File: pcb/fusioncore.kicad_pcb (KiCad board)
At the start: 2 copper layers, 95 x 99 mm, 116 parts, among them J1 40HAT, J10 Pump_Misc_1, J11 Pump_Misc_2, J12 I2C_DBG, J13 Conn_02x03_Top_Bottom, J14 LED, J15 Trigger, J16 WEIGHT, J17 Valve_M1, J18 Valve_M2, J19 Valve_M3, J2 Conn_02x12_Top_Bottom, J20 Valve_M4, J21 Valve_Air_Lime, J22 Valve_Air_Rum, J23 Valve_Air_Out, J3 Flow_Warm, J4 Temperature, J5 Flow_Cold, J6 CONN_01X02, J7 Pump_Cold, J8 Pump_Warm, J9 Pump_Air, Q1 DMG2305UX, Q10 AO3400A, Q11 AO3400A, Q2 DMMT5401, Q3 AO3400A, Q4 AO3400A, Q5 AO3400A, Q6 AO3400A, Q7 AO3400A, Q8 MMBT4403, Q9 AO3400A, SW1 POWER_ON, U1 CAT24C32, U2 INA226, U3 INA226, U4 INA226, U5 TXB0108DQSR, U6 HX711, U7 P82B96

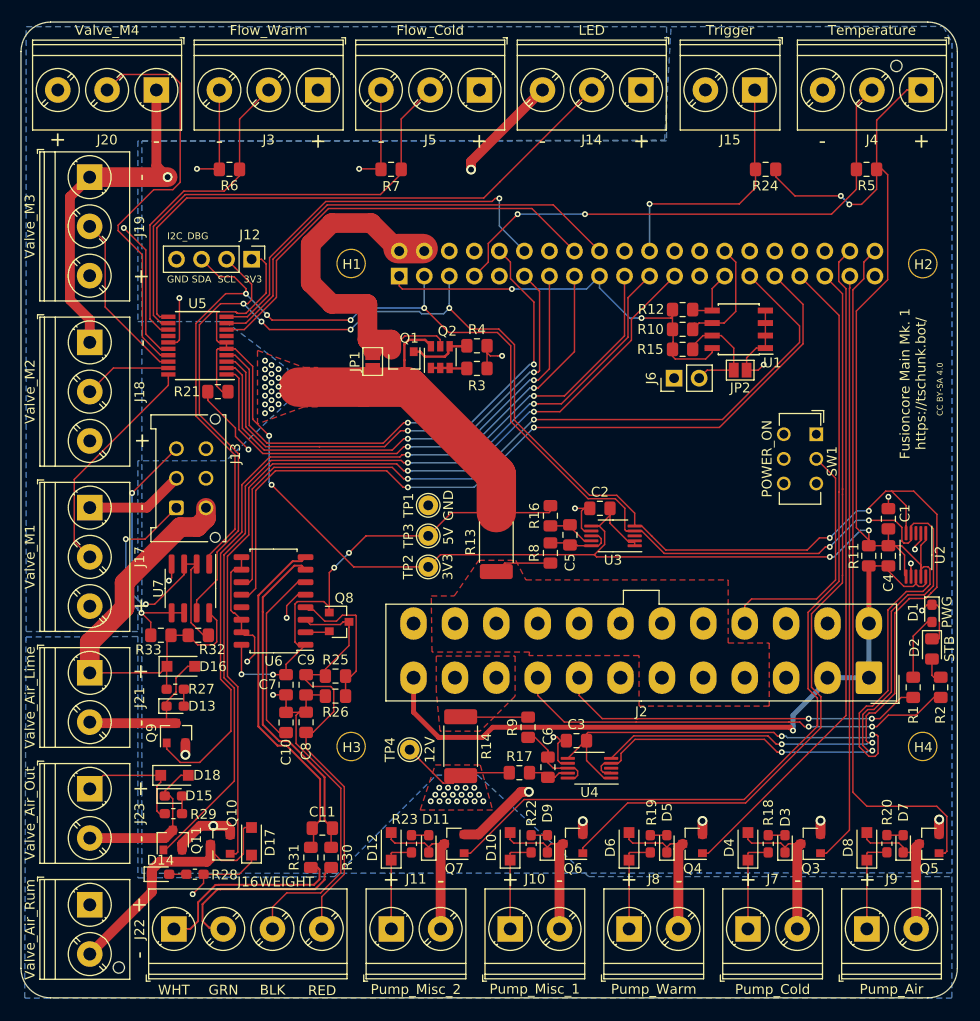
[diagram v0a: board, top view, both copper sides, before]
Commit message: Fixed issues from review.
Swapped diodes for Schottky diodes.
Changed logic level from HX711 to 3V3
Moved OE from 5V shifter to raspberry pi.
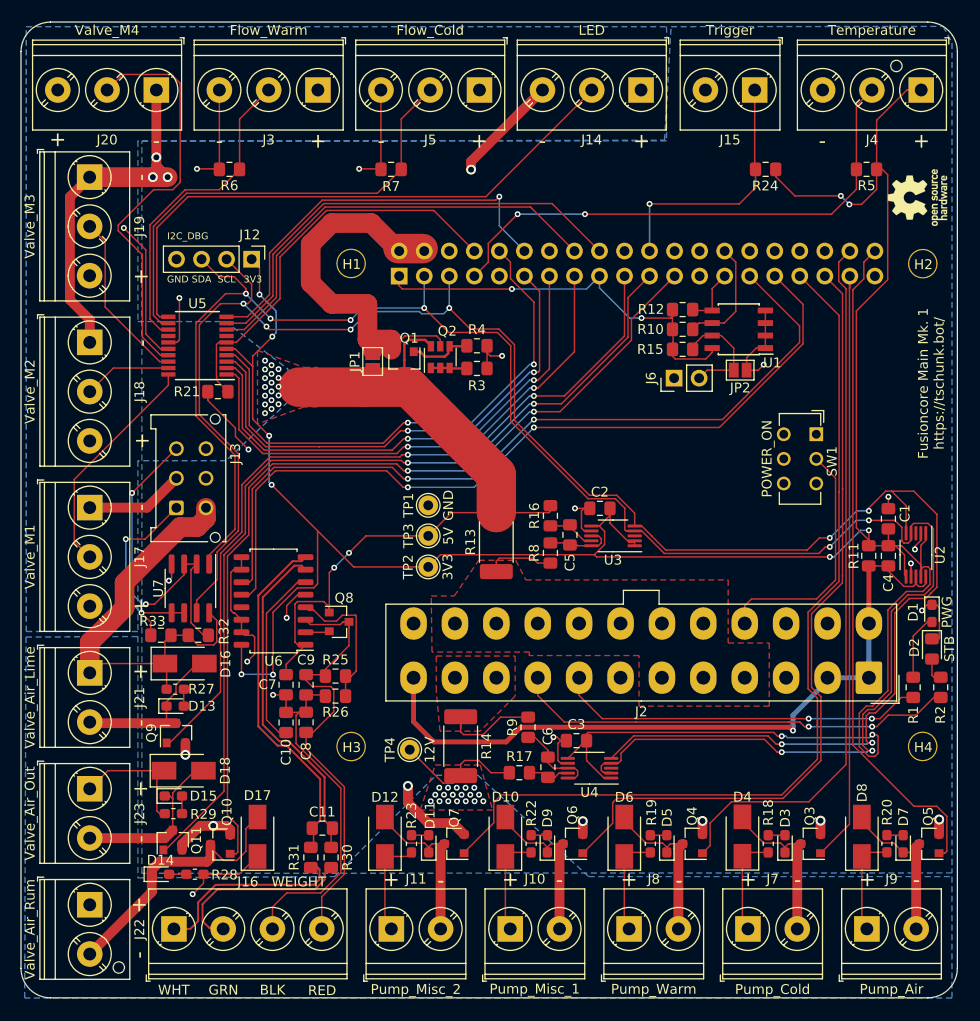
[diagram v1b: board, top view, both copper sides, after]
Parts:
- added REF**: OSHW-Logo_5.7x6mm_SilkScreen, Symbol:OSHW-Logo_5.7x6mm_SilkScreen, F.Cu at (139.5, 57.6)
- D10, D12, D16, D17, D18, D4, D6, D8: footprint Diode_SMD:D_SOD-123F -> Diode_SMD:D_SMA
- R1: value 150 -> 100
- moved D12 1.16 mm to (85.5, 122.5)
- moved D4 1.14 mm to (121.7, 122.5)
- moved D8 1.10 mm to (133.9, 122.5)
- moved D10 1.09 mm to (97.7, 122.5)
- moved D6 1.09 mm to (109.8, 122.5)
- moved D18 1.05 mm to (65.1, 115.8)
- moved D17 0.77 mm to (72.5, 122.5)
- moved D16 0.48 mm to (65.2, 104.9)
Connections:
- J1 pad 8: (no net) -> /EN_5V
- R21 pad 2: /3V3 -> /EN_5V
- U5 pad 6: /3V3 -> /EN_5V
- U6 pad 16: /5V -> /3V3
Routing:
- net /EN_5V: track 0.00 -> 41.8 mm
- net /3V3: track 266.8 -> 282.2 mm, vias 8 -> 12
- net /12V: track 128.6 -> 138.4 mm
- net /5V: track 99.5 -> 91.8 mm, vias 23 -> 21
- net /Valve_AL: track 86.5 -> 80.7 mm
- net /Pump_WW: track 68.2 -> 72.5 mm
- net /12V_ATX: track 6.86 -> 10.5 mm
- net /Pump_M2: track 90.9 -> 94.1 mm
- net /Pump_M1: track 78.2 -> 81.0 mm
- net /Pump_A: track 70.8 -> 68.0 mm
- net Net-(D14-Pad1): track 27.0 -> 28.3 mm
- net Net-(D11-Pad1): track 15.9 -> 17.0 mm
- net Net-(D15-Pad1): track 16.4 -> 17.5 mm
- net Net-(D3-Pad1): track 15.9 -> 16.9 mm
- net /5V_ATX: track 5.84 -> 6.87 mm
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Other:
- board text removed: "CC BY-SA 4.0"

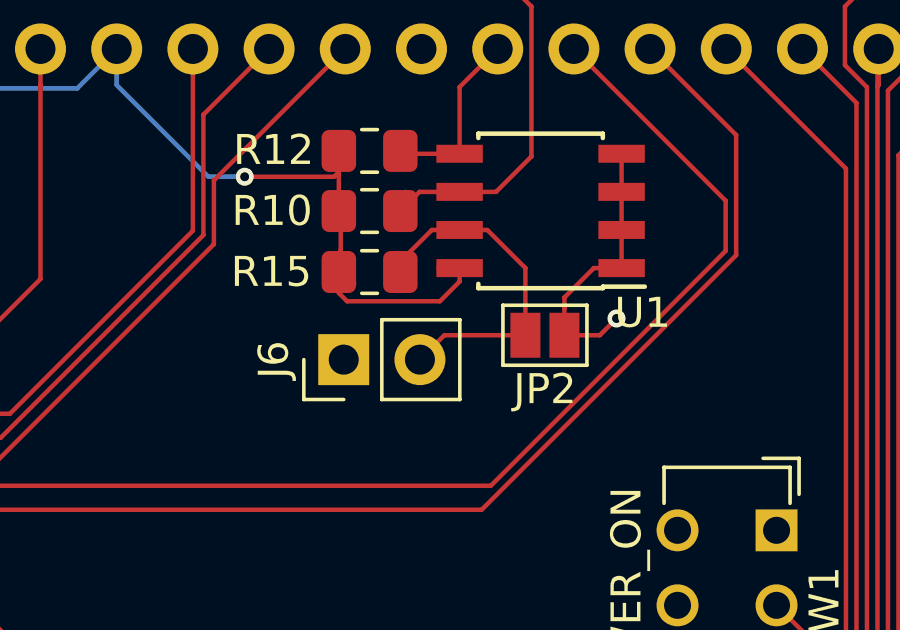
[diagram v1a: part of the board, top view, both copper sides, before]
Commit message: Simplified the EEPROM by removing an unecessary jumper
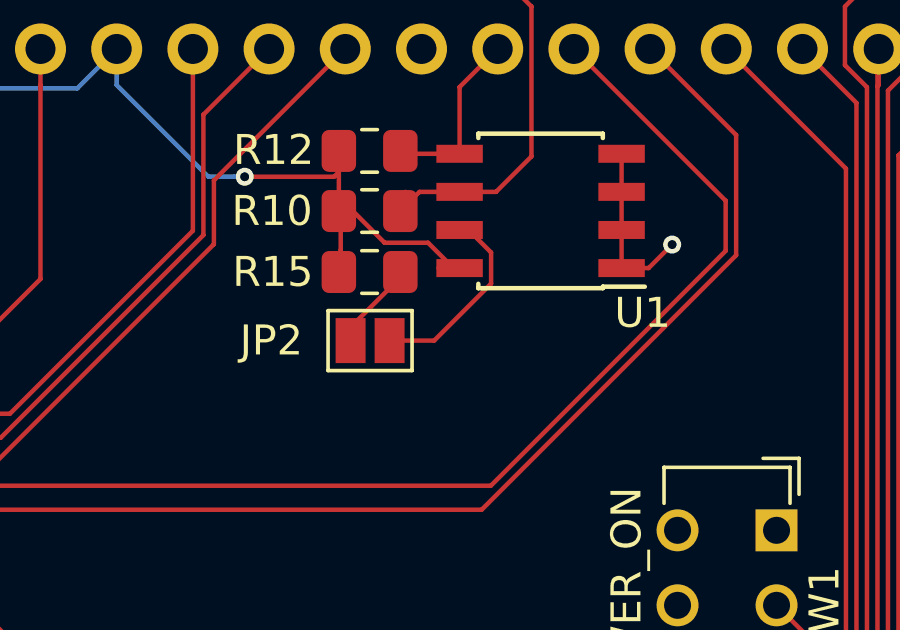
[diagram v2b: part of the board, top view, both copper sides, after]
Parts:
- removed J6: CONN_01X02, Connector_PinHeader_2.54mm:PinHeader_1x02_P2.54mm_Vertical
- moved JP2 5.83 mm to (115.7, 75.3), turned to 0 degrees
- turned R15 to 180 degrees
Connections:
- JP2 pad 1: GND -> Net-(JP2-Pad1)
- JP2 pad 2: Net-(J6-Pad2) -> Net-(JP2-Pad2)
- R15 pad 1: /3V3_PI -> Net-(JP2-Pad1)
- R15 pad 2: Net-(J6-Pad2) -> /3V3_PI
- U1 pad 7: Net-(J6-Pad2) -> Net-(JP2-Pad2)
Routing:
- net Net-(J6-Pad2): track 12.2 -> 0.00 mm
- net Net-(JP2-Pad2): track 0.00 -> 7.20 mm
- net GND: track 203.9 -> 200.4 mm
- net Net-(JP2-Pad1): track 0.00 -> 3.32 mm
- net /3V3_PI: track 43.6 -> 42.2 mm

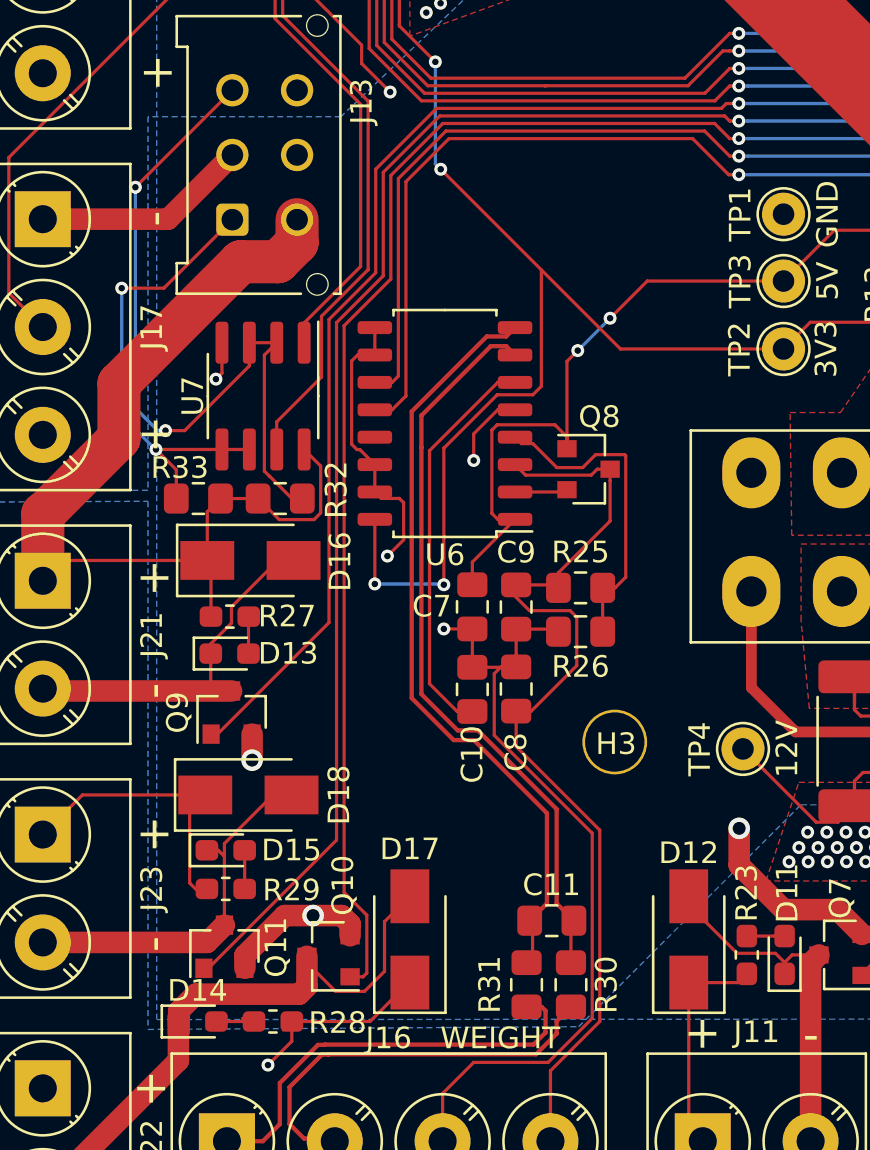
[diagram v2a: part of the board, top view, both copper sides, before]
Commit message: Added B+/- weight connector
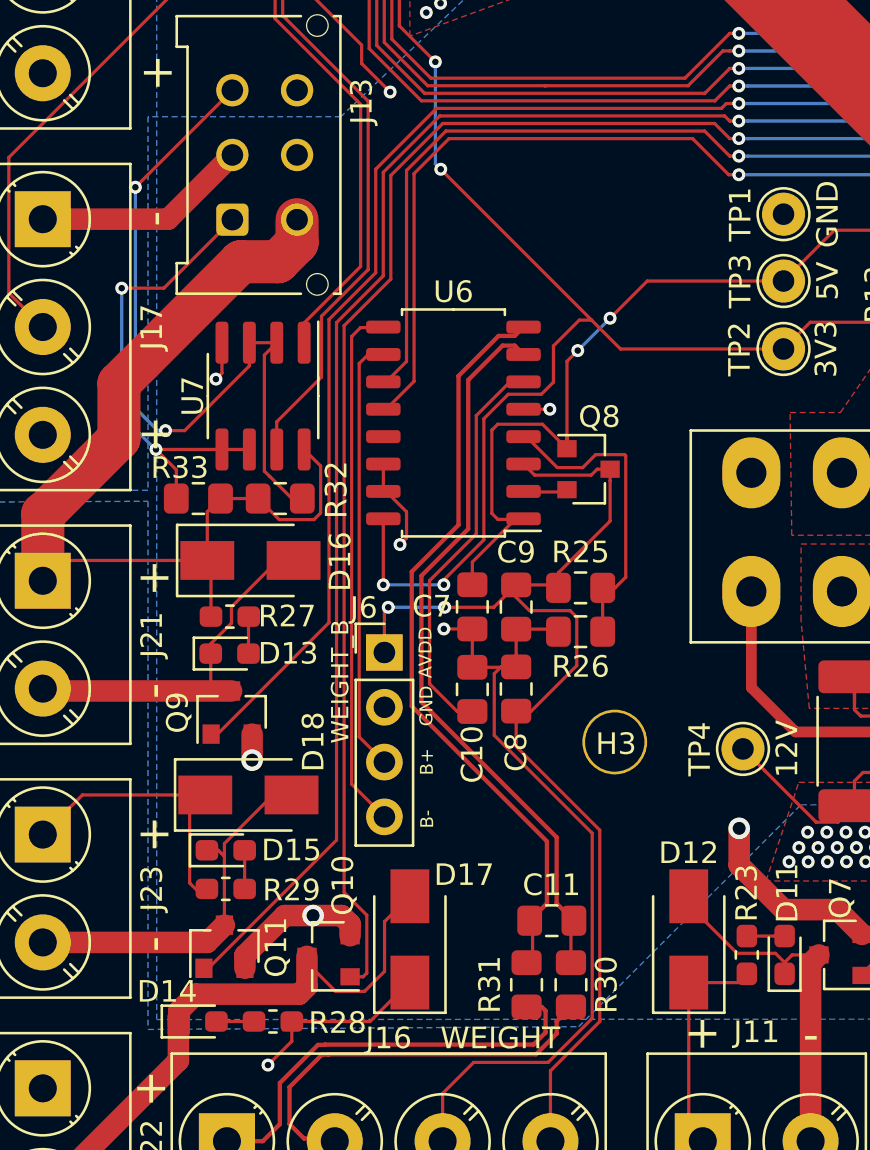
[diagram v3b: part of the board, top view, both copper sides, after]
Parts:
- added J6: WEIGHT_B, Connector_PinHeader_2.54mm:PinHeader_1x04_P2.54mm_Vertical, F.Cu at (71.4, 109.2)
- moved U6 0.39 mm to (74.6, 98.5)
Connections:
- U6 pad 10: GND -> /INB+
- U6 pad 9: GND -> /INB-
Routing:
- net /INB-: track 0.00 -> 24.4 mm
- net /INB+: track 0.00 -> 20.3 mm
- net GND: track 200.4 -> 189.0 mm
- net Net-(C8-Pad2): track 45.9 -> 54.1 mm, vias 0 -> 2
- net /3V3: track 282.2 -> 280.8 mm
- net /Weight_D: track 82.8 -> 82.2 mm
- net /Weight_CLK: track 81.9 -> 81.3 mm
- net Net-(D14-Pad2): track 2.27 -> 1.74 mm
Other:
- board text added: "AVDD"
- board text added: "B+"
- board text added: "B-"

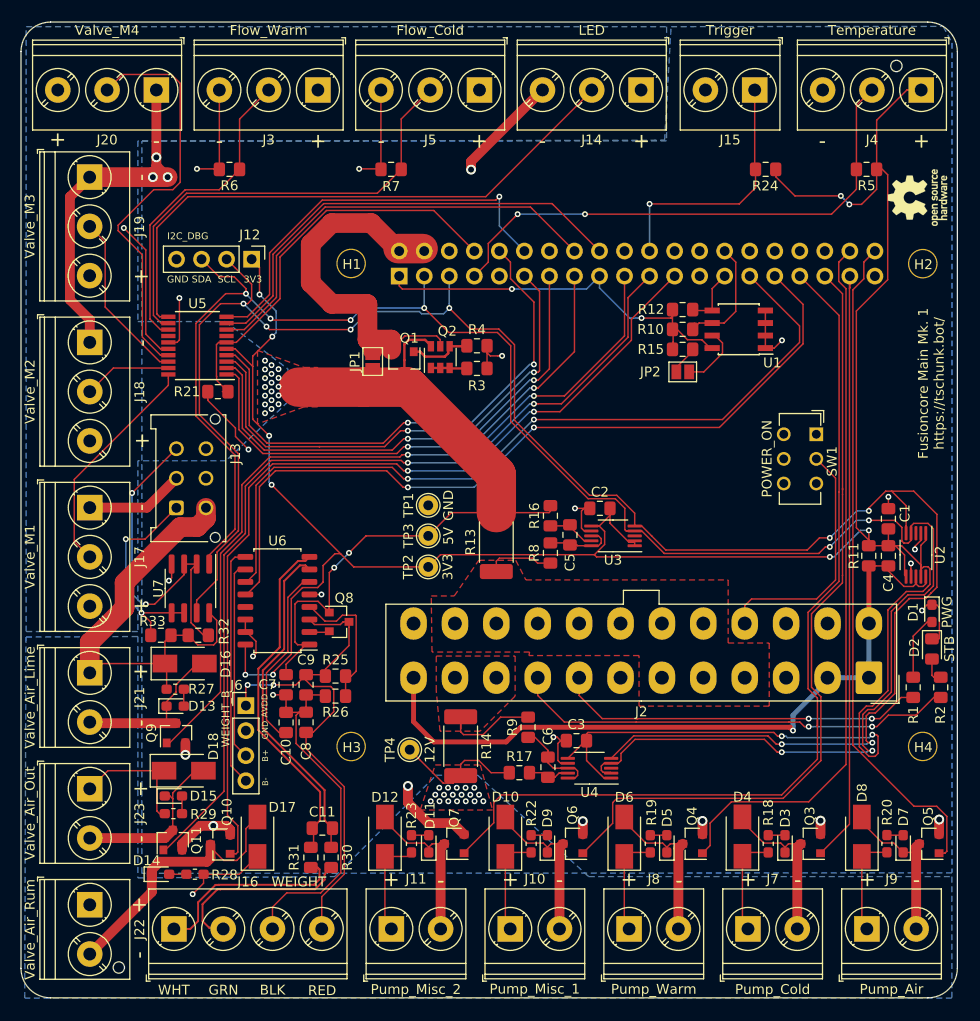
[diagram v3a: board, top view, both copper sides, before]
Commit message: Added relais for cooling compressor
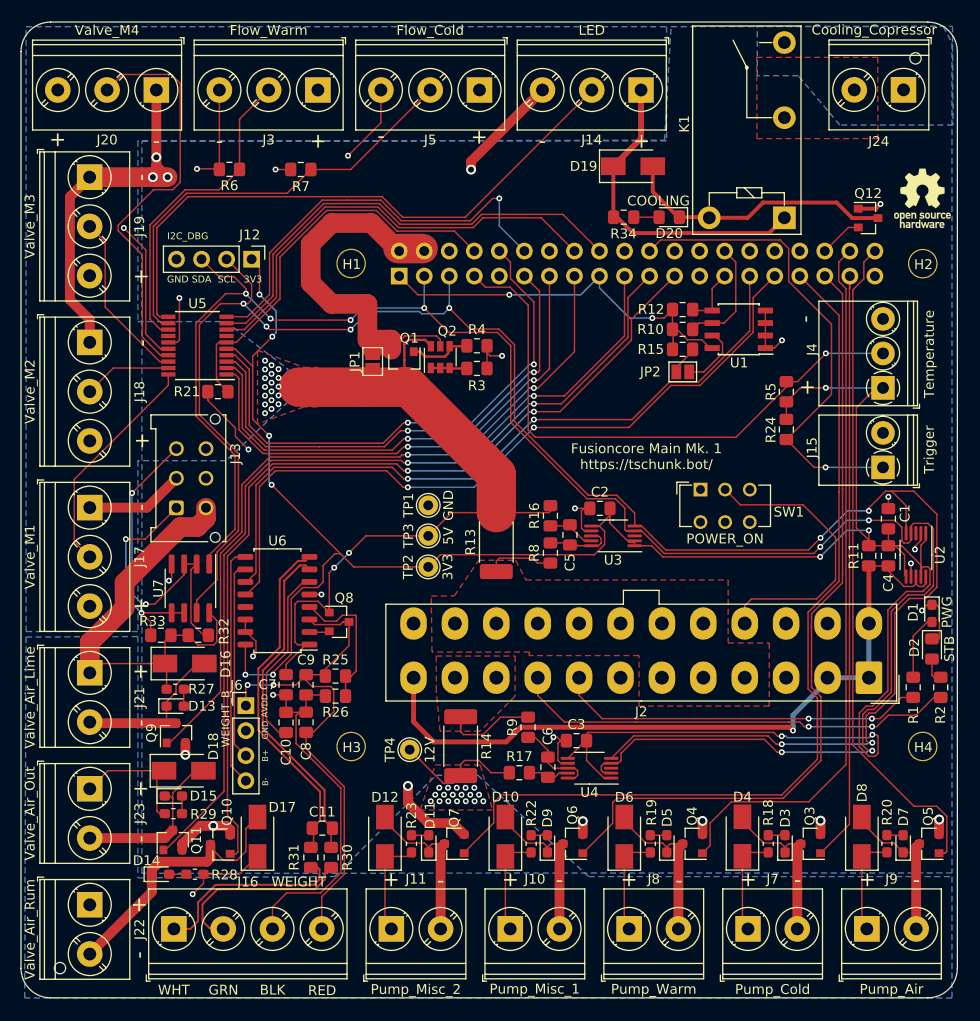
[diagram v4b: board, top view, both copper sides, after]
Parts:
- added D19: D, Diode_SMD:D_SMA, F.Cu at (110.6, 54.4)
- added D20: COOLING, LED_SMD:LED_0805_2012Metric_Pad1.15x1.40mm_HandSolder, F.Cu at (114.3, 59.6)
- added J24: Cooling_Copressor, TerminalBlock_Phoenix:TerminalBlock_Phoenix_PT-1,5-2-5.0-H_1x02_P5.00mm_Horizontal, F.Cu at (138.1, 46.7)
- added K1: G5Q-1A, Relay_THT:Relay_SPST_Omron-G5Q-1A, F.Cu at (126.0, 59.7)
- added Q12: 2N3904, Package_TO_SOT_SMD:SOT-23, F.Cu at (134.5, 59.7)
- added R34: 150, Resistor_SMD:R_0805_2012Metric_Pad1.15x1.40mm_HandSolder, F.Cu at (109.7, 59.6)
- J15: footprint TerminalBlock_Phoenix:TerminalBlock_Phoenix_PT-1,5-2-5.0-H_1x02_P5.00mm_Horizontal -> project_footprints:TerminalBlock_Phoenix_PT-1,5-2-3.5-H_1x02_P3.50mm_Diagonal
- J4: footprint TerminalBlock_Phoenix:TerminalBlock_Phoenix_PT-1,5-3-5.0-H_1x03_P5.00mm_Horizontal -> project_footprints:TerminalBlock_Phoenix_PT-1,5-2-3.5-H_1x03_P3.50mm_Diagonal
- moved J15 40.4 mm to (136.0, 85.0), turned to 90 degrees
- moved J4 30.5 mm to (136.0, 76.9), turned to 90 degrees
- moved R24 26.5 mm to (126.2, 81.2), turned to 90 degrees
- moved R5 24.0 mm to (126.2, 77.3), turned to 90 degrees
- moved SW1 13.0 mm to (117.5, 87.2), turned to 0 degrees
- moved R7 9.16 mm to (76.9, 54.8)
- moved H5 5.97 mm to (52.5, 135.8)
- moved H6 2.09 mm to (139.3, 43.5)
- moved REF** 0.51 mm to (140.0, 57.7), turned to 0 degrees
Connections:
- J1 pad 36: (no net) -> /Cooler
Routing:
- net /3V3: track 280.8 -> 240.9 mm, vias 12 -> 11
- net /5V: track 92.1 -> 124.8 mm
- net Net-(D19-Pad2): track 0.00 -> 27.8 mm
- net /Trigger: track 26.2 -> 49.0 mm
- net /Weight_CLK: track 81.3 -> 73.4 mm
- net /Weight_D: track 82.2 -> 76.2 mm
- net /1W: track 54.2 -> 59.5 mm, vias 2 -> 1
- net /PS_ON: track 25.2 -> 29.6 mm
- net /Cooler: track 0.00 -> 4.39 mm
- net /Flow_C_5V: track 48.1 -> 44.7 mm
- net Net-(D20-Pad2): track 0.00 -> 2.57 mm
- net GND: track 189.0 -> 191.0 mm, vias 27 -> 29
- net /LED_PWM_5V: track 60.0 -> 61.7 mm
- net /LED_PWM: track 41.6 -> 43.3 mm
- net /Flow_W: track 44.8 -> 45.6 mm
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- added copper zone on B.Cu, net Net-(J24-Pad1)
- added copper zone on F.Cu, net Net-(J24-Pad2)
